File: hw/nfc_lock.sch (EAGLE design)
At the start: 30 parts, among them IC1 STM8S003F3, IC3 MCP170312MB, Q1 8MHz, Q3 2N7002,215, U1 M24SR16-YMN6T/2, U2 IRFML8244TRPBF, U3 IRFML8244TRPBF, X1 MINI-USB-32005-301

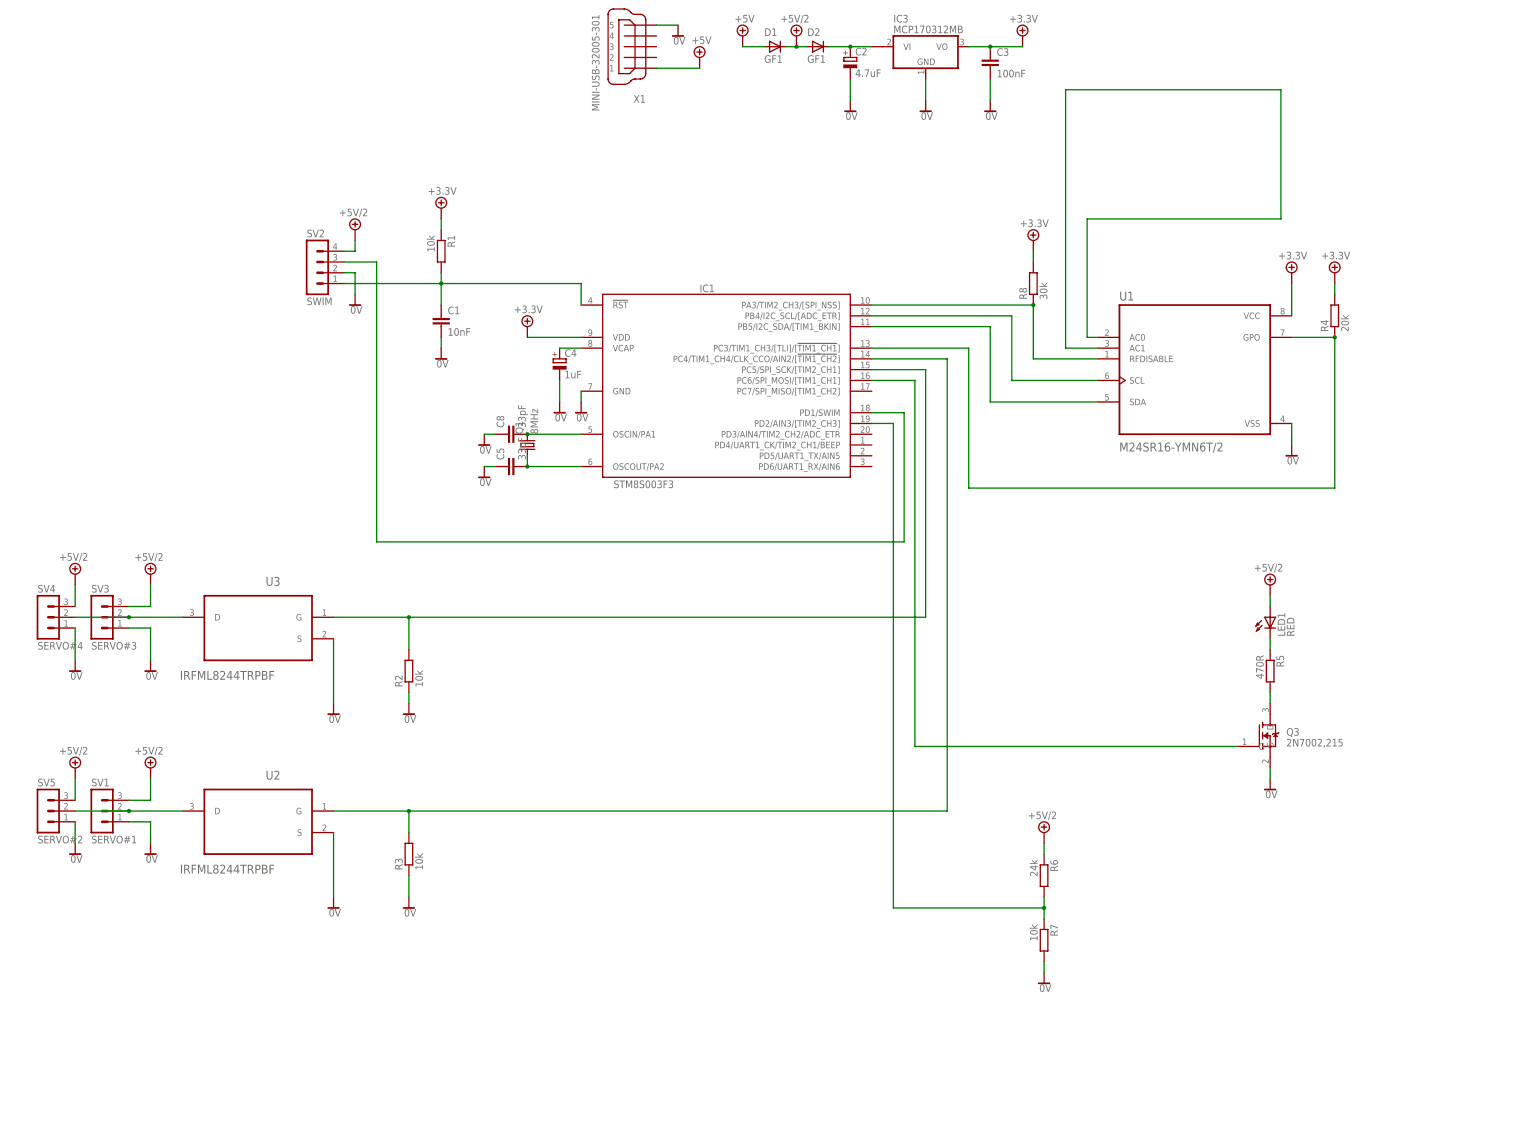
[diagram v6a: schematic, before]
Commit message: added on/off transistor for servos. replaced transistor for PWM servo control. added names to the most important signal lines.
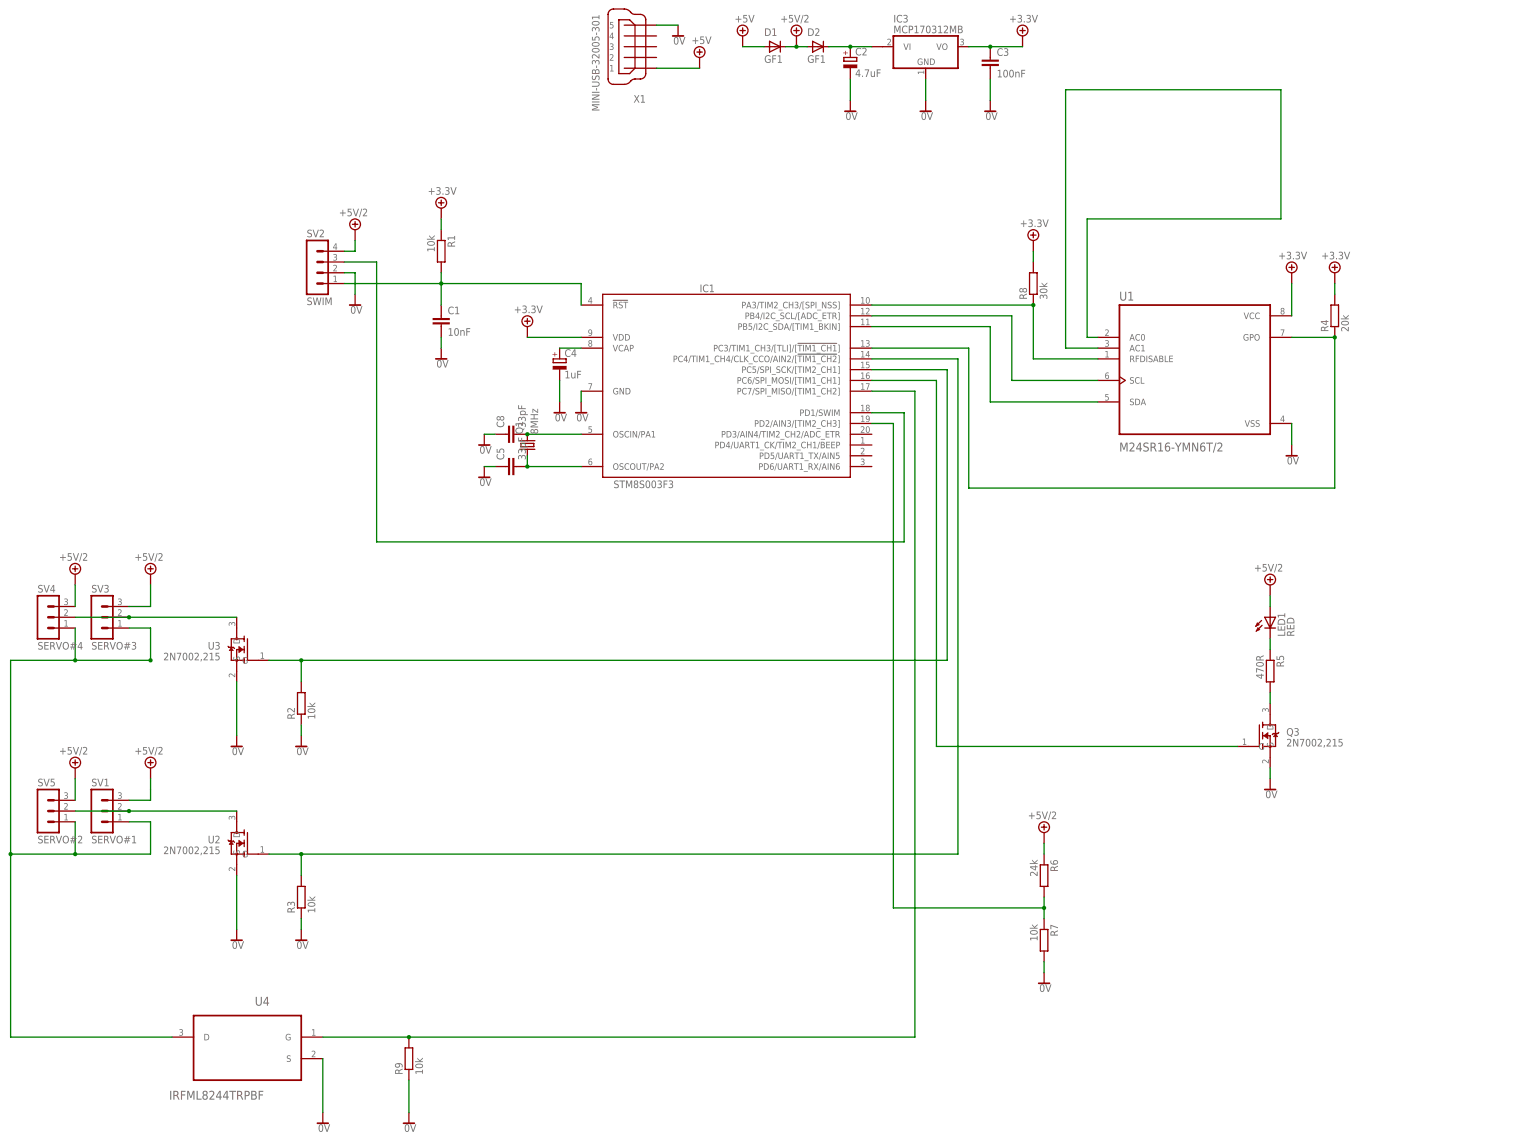
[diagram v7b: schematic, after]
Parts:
- added R9: 10k, rcl:R-EU_R0805
- added U4: IRFML8244TRPBF, irfml8244trpbf:IRFML8244TRPBF
- U2, U3: value IRFML8244TRPBF -> 2N7002,215; device irfml8244trpbf:IRFML8244TRPBF -> Common-Parts-Library-Eagle:2N7002,215
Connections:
- net N$1 renamed SCL
- net N$13 renamed SERVO_PACK_2
- net N$19 renamed CTRL_LED
- net N$2 renamed SDA
- net N$3 renamed SERVO_PACK_1
- new net SERVO_GND: SV1.1, SV3.1, SV4.1, SV5.1, U4.D
- new net SERWO_PWR: IC1.PC7/SPI_MISO/[TIM1_CH2], R9.2, U4.G
- net 0V: now also R9.1, U4.S; no longer SV1.1, SV3.1, SV4.1, SV5.1
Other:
- moved on the sheet: R2, R3
